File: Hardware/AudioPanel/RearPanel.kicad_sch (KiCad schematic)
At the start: 20 parts, among them J1 PWR IN, J12 COM Port, J13 COM Port, J14 COM Port, J15 COM Port, J17 MIC Port, J18 Speakers, J19 DATA Port, J21 MIC Port, J22 Speakers, J23 DATA Port, J25 GPS IN, J26 DATA Port, J29 MIC Port, J3 MIC Port, J30 Speakers, J31 DATA Port, J5 AudioJack2, J6 RCA x6, J8 RCA x6

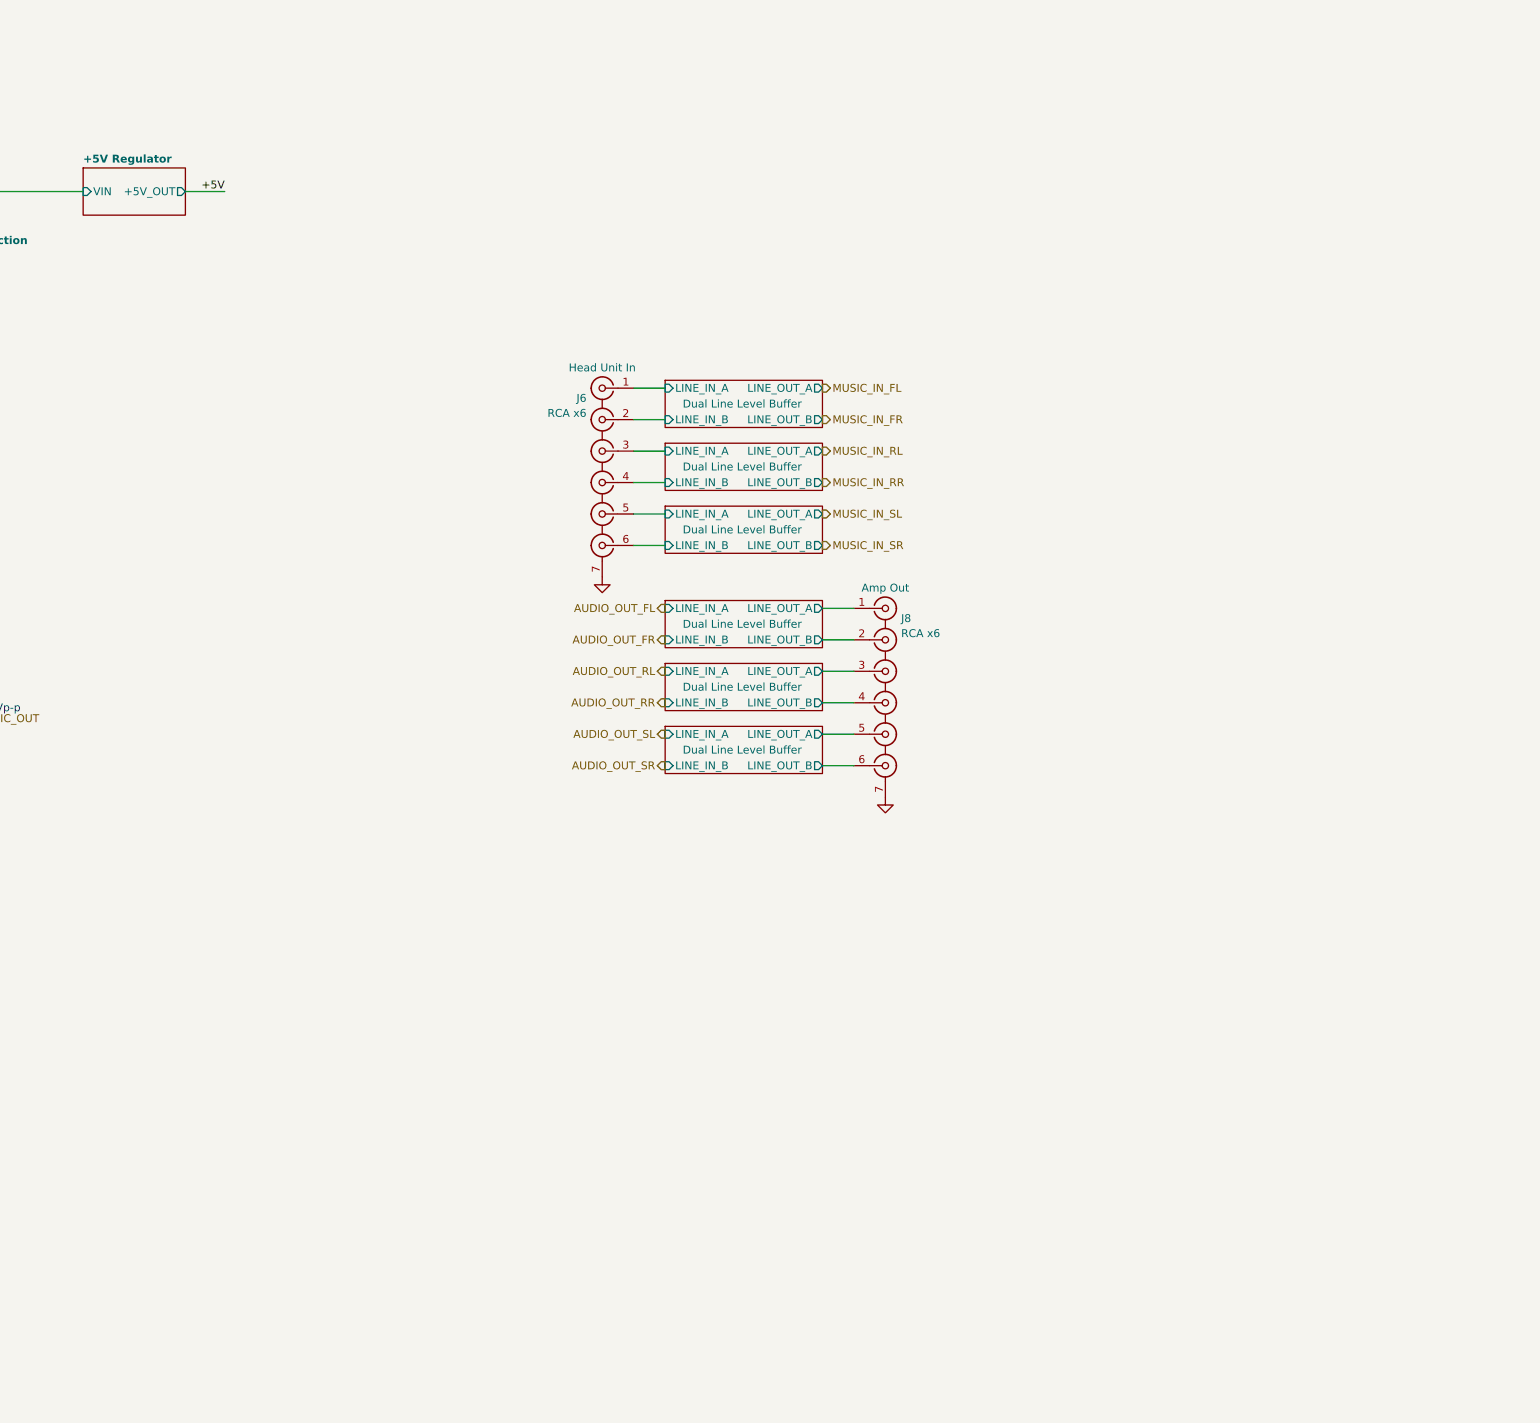
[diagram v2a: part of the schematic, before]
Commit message: Added initial DB audio out connector
Need to pick the best way to convert single-ended audio to differential
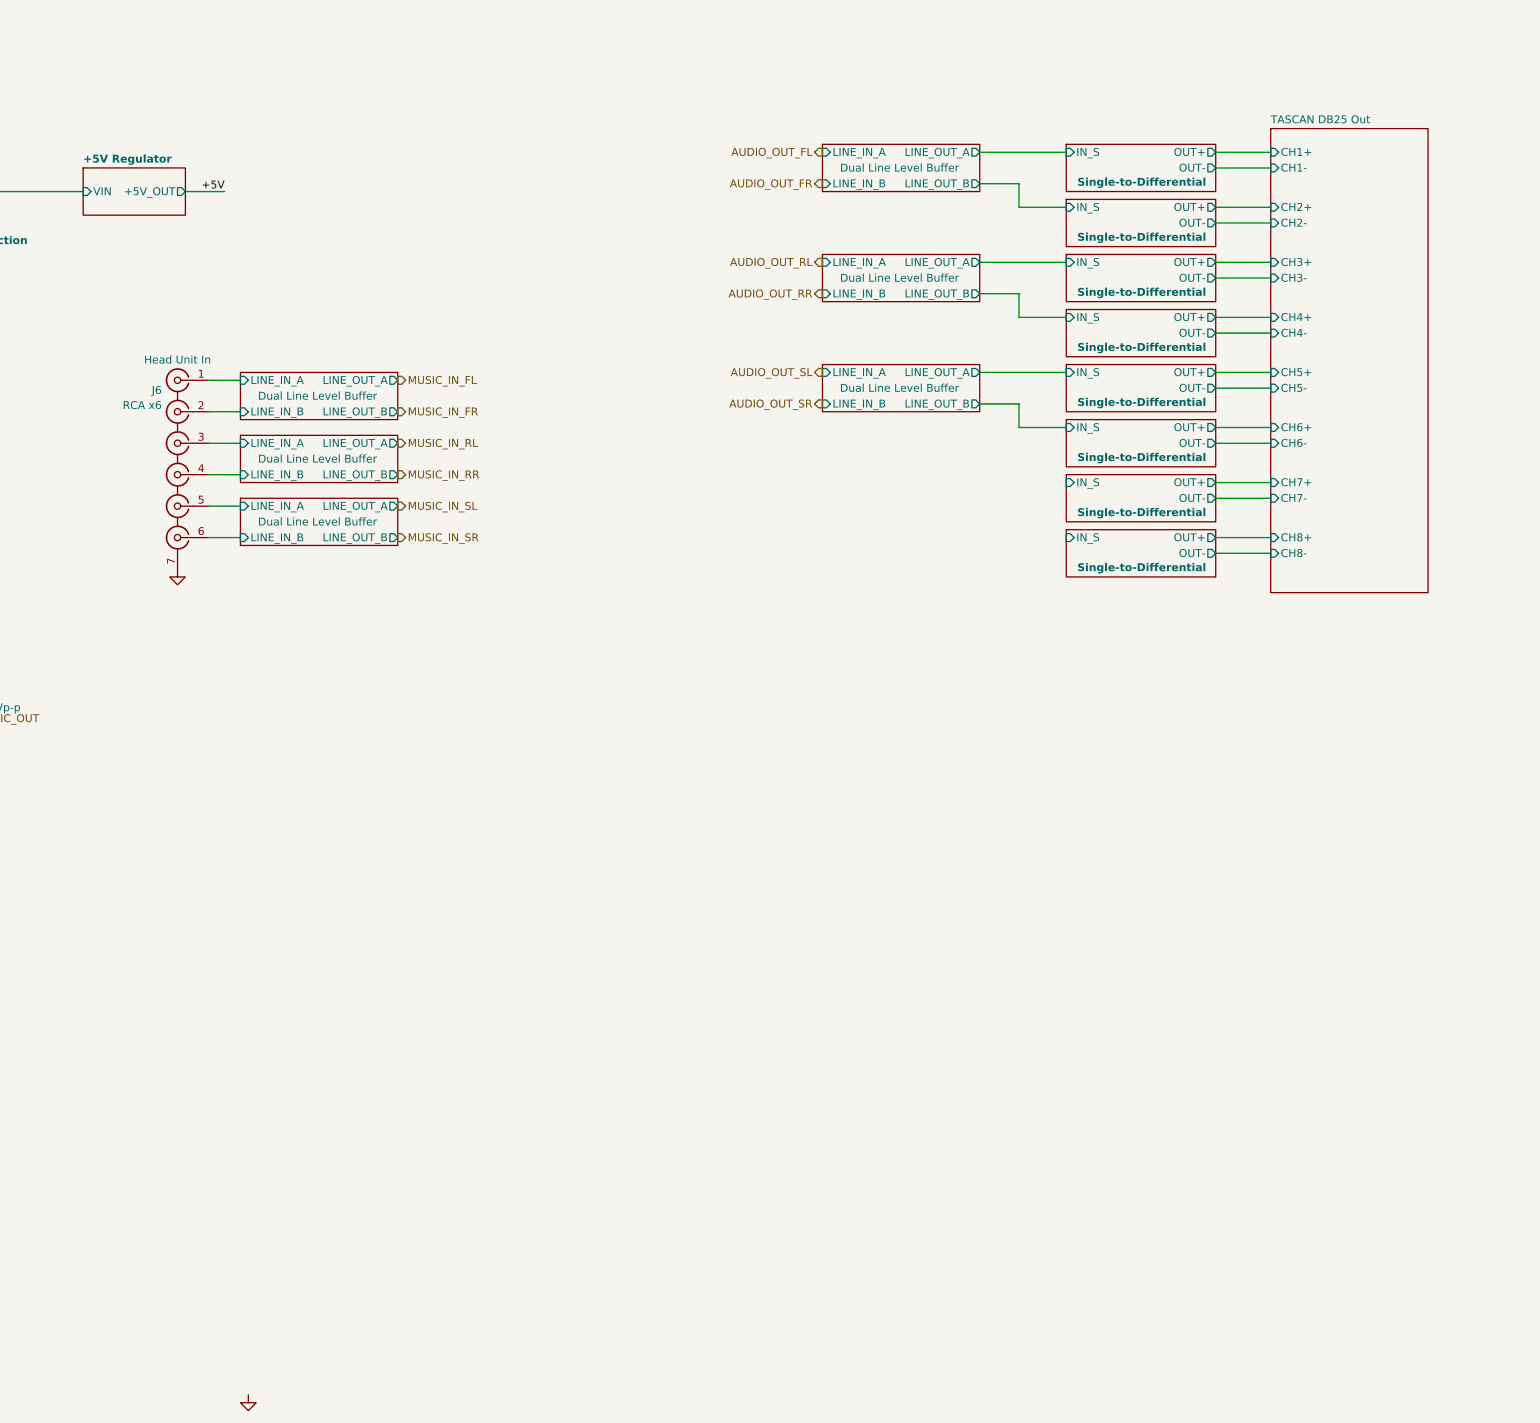
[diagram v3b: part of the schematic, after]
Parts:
- removed J8: RCA x6, symbol Connector:Conn_Coaxial_x2
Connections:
- net Dual Line Level Buffer/LINE_IN_A is gone; now on net Dual Line Level Buffer/LINE_IN_A: J6.5 (IN2)
- net Dual Line Level Buffer/LINE_IN_B is gone; now on net Dual Line Level Buffer/LINE_IN_B: J6.6 (IN2)
- net Dual Line Level Buffer/LINE_IN_A: no longer J6.1 (IN1)
- net Dual Line Level Buffer/LINE_IN_B: no longer J6.2 (IN2)
- new net Dual Line Level Buffer/LINE_IN_A: J6.1 (IN1)
- new net Dual Line Level Buffer/LINE_IN_B: J6.2 (IN2)
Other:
- added sheet Single-to-Differential (SINGLE-DIFF.kicad_sch)
- added sheet TASCAN DB25 Out (TASCAN_AUDIO_OUT.kicad_sch)
- moved on the sheet: J6

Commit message: Realized that I need to rethink how I'm going to mix the radio audio with the stereo audio
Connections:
- net Dual Line Level Buffer/LINE_IN_A is gone; now on net Dual Line Level Buffer/LINE_IN_A: J6.5 (IN2)
- net Dual Line Level Buffer/LINE_IN_B is gone; now on net Dual Line Level Buffer/LINE_IN_B: J6.6 (IN2)
- net Dual Line Level Buffer/LINE_IN_A: no longer J6.1 (IN1)
- net Dual Line Level Buffer/LINE_IN_B: no longer J6.2 (IN2)
- new net Dual Line Level Buffer/LINE_IN_A: J6.1 (IN1)
- new net Dual Line Level Buffer/LINE_IN_B: J6.2 (IN2)

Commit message: Added MT8816 for audio switching
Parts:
- added J32: Speakers, symbol Connector_Generic:Conn_01x02
- added J34, J9: Speakers, symbol Connector_Generic:Conn_01x03
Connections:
- net Dual Line Level Buffer/LINE_IN_A is gone; now on net Dual Line Level Buffer/LINE_IN_A: J6.5 (IN2)
- net Dual Line Level Buffer/LINE_IN_B is gone; now on net Dual Line Level Buffer/LINE_IN_B: J6.6 (IN2)
- net Dual Line Level Buffer/LINE_IN_A: no longer J6.1 (IN1)
- net Dual Line Level Buffer/LINE_IN_B: no longer J6.2 (IN2)
- net D700_SPEAKER_1 renamed 700_SPKR1
- net D700_SPEAKER_2 renamed 700_SPKR2
- net D710_SPEAKER_1 renamed 710_SPKR1
- net D710_SPEAKER_2 renamed 710_SPKR2
- net TS480_SPEAKER_1 renamed 480_SPKR
- net TS480_SPEAKER_GND renamed 480_SPEAKER_GND
- new net Dual Line Level Buffer/LINE_IN_A: J6.1 (IN1)
- new net Dual Line Level Buffer/LINE_IN_B: J6.2 (IN2)
- new net EXTRA_SPEAKER_GND: J9.3 (Pin_3)
- new net EXTRA_SPKR1: J9.1 (Pin_1)
- new net EXTRA_SPKR2: J9.2 (Pin_2)
- new net RASPI_SPEAKER_GND: J34.3 (Pin_3)
- new net RASPI_SPKRL: J34.1 (Pin_1)
- new net RASPI_SPKRR: J34.2 (Pin_2)
- new net SCANNER_SPEAKER_GND: J32.2 (Pin_2)
- new net SCANNER_SPKR: J32.1 (Pin_1)
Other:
- added sheet TASCAN DB15 (TASCAN_AUDIO_OUT.kicad_sch)
- moved on the sheet: J18

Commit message: Added DATA switching to COM switching page
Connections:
- net Dual Line Level Buffer/LINE_IN_A is gone; now on net Dual Line Level Buffer/LINE_IN_A: J6.5 (IN2)
- net Dual Line Level Buffer/LINE_IN_B is gone; now on net Dual Line Level Buffer/LINE_IN_B: J6.6 (IN2)
- net Dual Line Level Buffer/LINE_IN_A: no longer J6.1 (IN1)
- net Dual Line Level Buffer/LINE_IN_B: no longer J6.2 (IN2)
- new net Dual Line Level Buffer/LINE_IN_A: J6.1 (IN1)
- new net Dual Line Level Buffer/LINE_IN_B: J6.2 (IN2)
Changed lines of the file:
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@@
 	)
 	(bus_alias "MUSIC_SE"
-		(members "HL" "HR" "ML" "MR" "LL" "LR")
+		(members "TSCL" "TSDA" "~{RESET}")
 	)
 	(text "MIC +- Signaling:\n4mVp-p"

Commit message: Cleaned up stuff, defined more busses
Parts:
- added C554: 100uF, symbol Device:C_Polarized_Small_US
- added C555: 10uF, symbol Device:C_Polarized_Small_US
- added C556: 4n7, symbol Device:C_Small
- added J16: USB_A, symbol Connector:USB_A
- added L34: 120R, symbol Device:L_Ferrite
- added U67: USBLC6-2SC6, Package_TO_SOT_SMD:SOT-23-6, symbol Power_Protection:USBLC6-2SC6
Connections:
- net Dual Line Level Buffer/LINE_IN_A is gone; now on net Dual Line Level Buffer/LINE_IN_A: J6.5 (IN2)
- net Dual Line Level Buffer/LINE_IN_B is gone; now on net Dual Line Level Buffer/LINE_IN_B: J6.6 (IN2)
- net Dual Line Level Buffer/LINE_IN_A: no longer J6.1 (IN1)
- net Dual Line Level Buffer/LINE_IN_B: no longer J6.2 (IN2)
- net GND: now also C554.2, C555.2, U67.2 (GND)
- new net: C556.1, J16.5 (Shield)
- new net: C556.2, J16.4 (GND)
- new net +5V_HOST: C554.1, L34.1, U67.5 (VBUS)
- new net +5V_HOST_FILT: C555.1, J16.1 (VBUS), L34.2
- new net Dual Line Level Buffer/LINE_IN_A: J6.1 (IN1)
- new net Dual Line Level Buffer/LINE_IN_B: J6.2 (IN2)
- new net USB_CONN_HOST_D+: U67.1 (I/O1)
- new net USB_CONN_HOST_D-: U67.3 (I/O2)
- new net USB_CONN_HOST_D_ESD+: J16.3 (D+), U67.6 (I/O1)
- new net USB_CONN_HOST_D_ESD-: J16.2 (D-), U67.4 (I/O2)
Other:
- removed sheet +5V Regulator
- sheet Input Power Protection ports: added none; removed +5V_IN

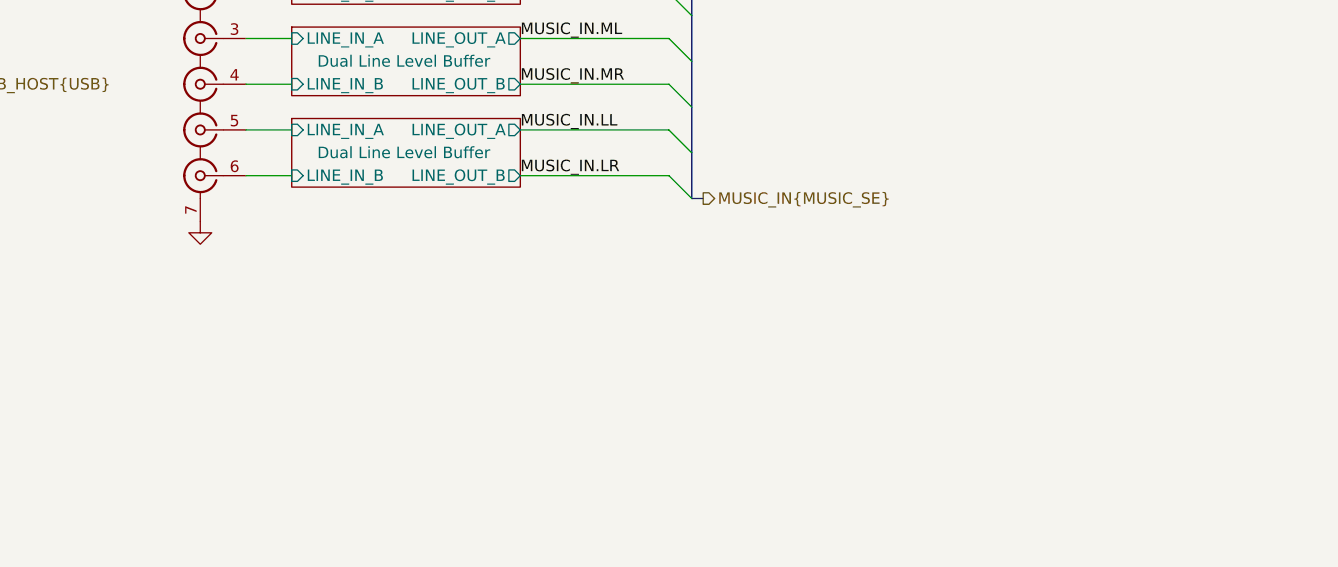
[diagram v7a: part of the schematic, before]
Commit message: Laid groundwork for stereo DSP routing
I figured it out. I need to combine the left audio channels, combine the right audio channels, pass both to the DSP chips. Each audio zone will eventually have its own DSP to handle crossovers and time delay and things.

Use the Pioneer Network Mode for easier frequency separation.

To do: add active summing amplifers to combine left and right sub-channels
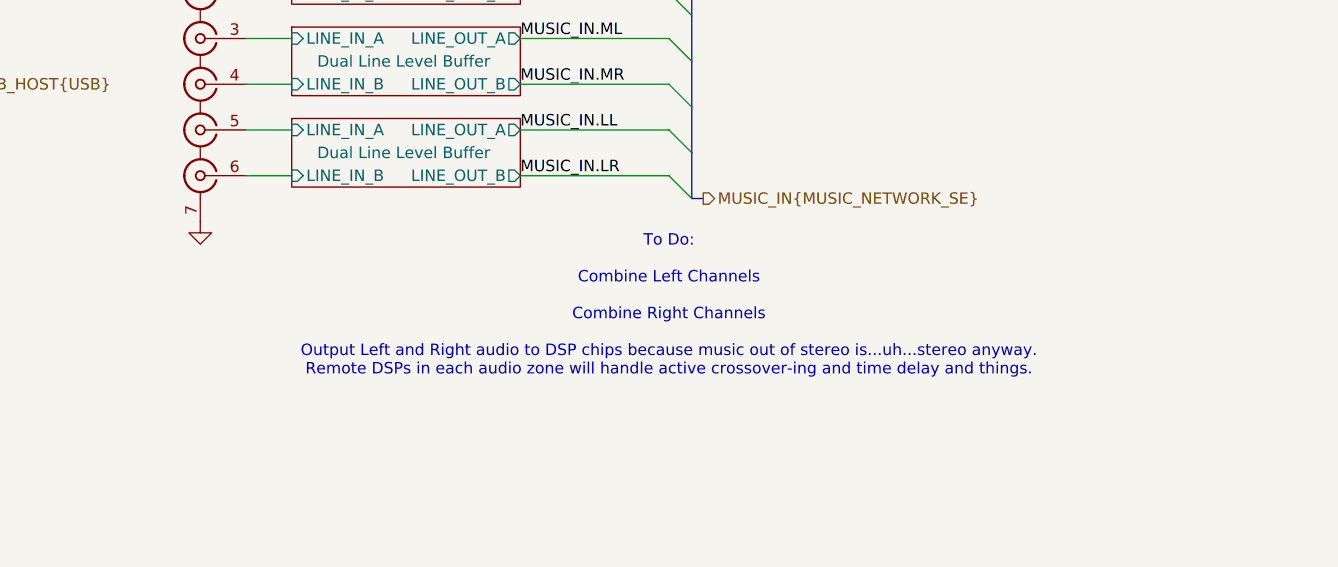
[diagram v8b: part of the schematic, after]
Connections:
- net Dual Line Level Buffer/LINE_IN_A is gone; now on net Dual Line Level Buffer/LINE_IN_A: J6.5 (IN2)
- net Dual Line Level Buffer/LINE_IN_B is gone; now on net Dual Line Level Buffer/LINE_IN_B: J6.6 (IN2)
- net Dual Line Level Buffer/LINE_IN_A: no longer J6.1 (IN1)
- net Dual Line Level Buffer/LINE_IN_B: no longer J6.2 (IN2)
- new net Dual Line Level Buffer/LINE_IN_A: J6.1 (IN1)
- new net Dual Line Level Buffer/LINE_IN_B: J6.2 (IN2)
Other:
- note added: "To Do: Combine Left Channels Combine Right Channels Output Left and Right audio to DSP chips because music out of stereo is...uh...stereo anyway. Remote DSPs in each audio zone will handle active crossover-ing and time delay and things."
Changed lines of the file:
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@@
 		(members "UP" "DOWN" "PTT" "+")
 	)
-	(bus_alias "MUSIC_LVDS"
+	(bus_alias "MUSIC_NETWORK_LVDS"
 		(members "HL+" "HL-" "HR+" "HR-" "ML+" "ML-" "MR+" "MR-" "LL+" "LL-" "LR+"
 			"LR-"
 		)
 	)
-	(bus_alias "MUSIC_SE"
-		(members "TSCL" "TSDA" "~{RESET}")
+	(bus_alias "MUSIC_STANDARD_LVDS"
+		(members "FR+" "FR-" "FL+" "FL-" "RR+" "RR-" "RL+" "RL-" "SR+" "SR-" "SL+"
+			"SL-"
+		)
+	)
+	(bus_alias "MUSIC_STANDARD_SE"
+		(members "FL" "FR" "RL" "RR" "SL" "SR")
 	)
 	(bus_alias "USB"
-		(members "D+" "D-")
+		(members "HL+" "HL-" "HR+" "HR-" "ML+" "ML-" "MR+" "MR-" "LL+" "LL-" "LR+"
+			"LR-"
+		)
 	)
 	(text "MIC +- Signaling:\n4mVp-p"
@@
 		)
 	)
+	(text "To Do:\n\nCombine Left Channels\n\nCombine Right Channels\n\nOutput Left and Right audio to DSP chips because music out of stereo is...uh...stereo anyway.\nRemote DSPs in each audio zone will handle active crossover-ing and time delay and things."
+		(exclude_from_sim no)
+		(at 243.84 231.648 0)
+		(effects
+			(font
+				(size 1.27 1.27)
+			)
+		)
+	)
 	(text "2Vp-p"
 		(exclude_from_sim no)
@@
 		)
 	)
-	(hierarchical_label "MUSIC_IN{MUSIC_SE}"
+	(hierarchical_label "MUSIC_IN{MUSIC_NETWORK_SE}"
 		(shape output)
 		(at 247.65 219.71 0)
